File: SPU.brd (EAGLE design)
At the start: 160 x 130 mm, 421 parts, among them Q1 BSS123, Q2 12MHz, Q3 BSS123, Q4 BSS123, Q5 BSS123, Q6 BSS123, Y1 32.768kHz

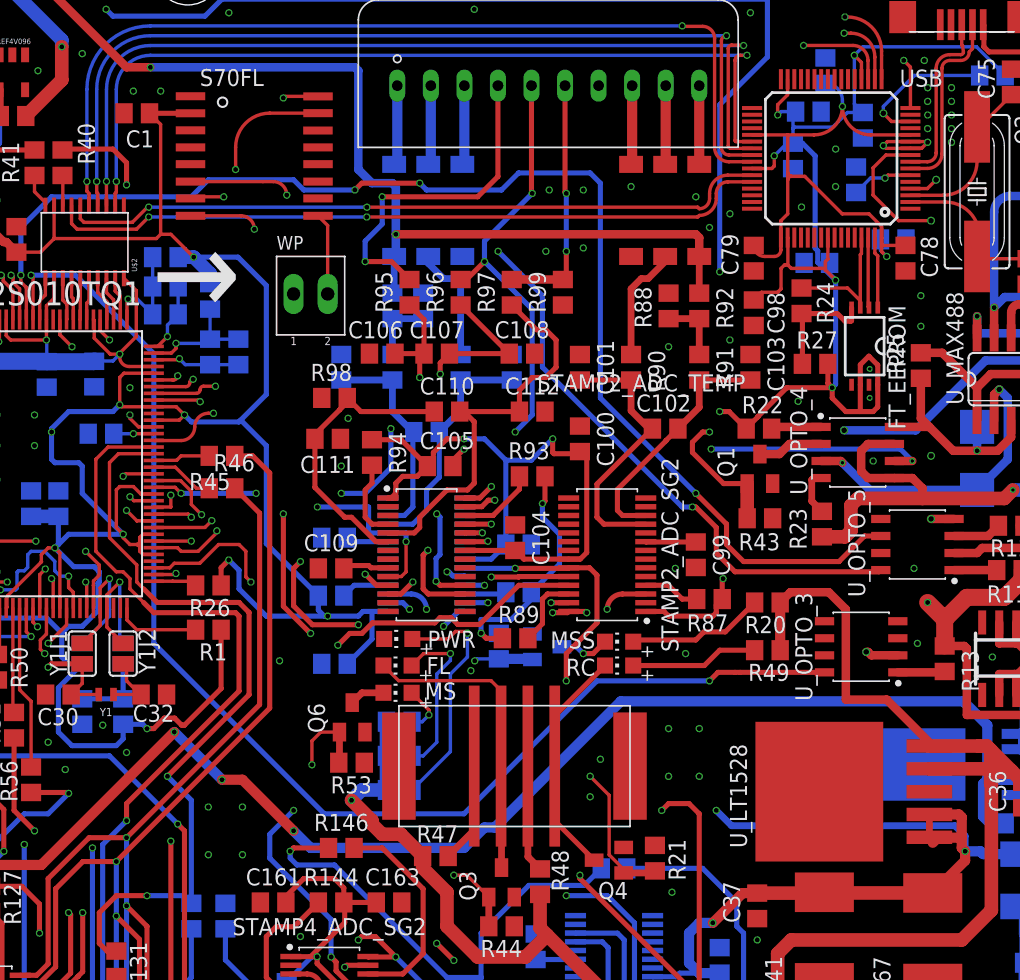
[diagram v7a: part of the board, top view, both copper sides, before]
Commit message: Minor changes
- XTAL from AUX to MAIN
- Removes authors
- Adds interface measurements
- Fixes Airwire / Wirestub
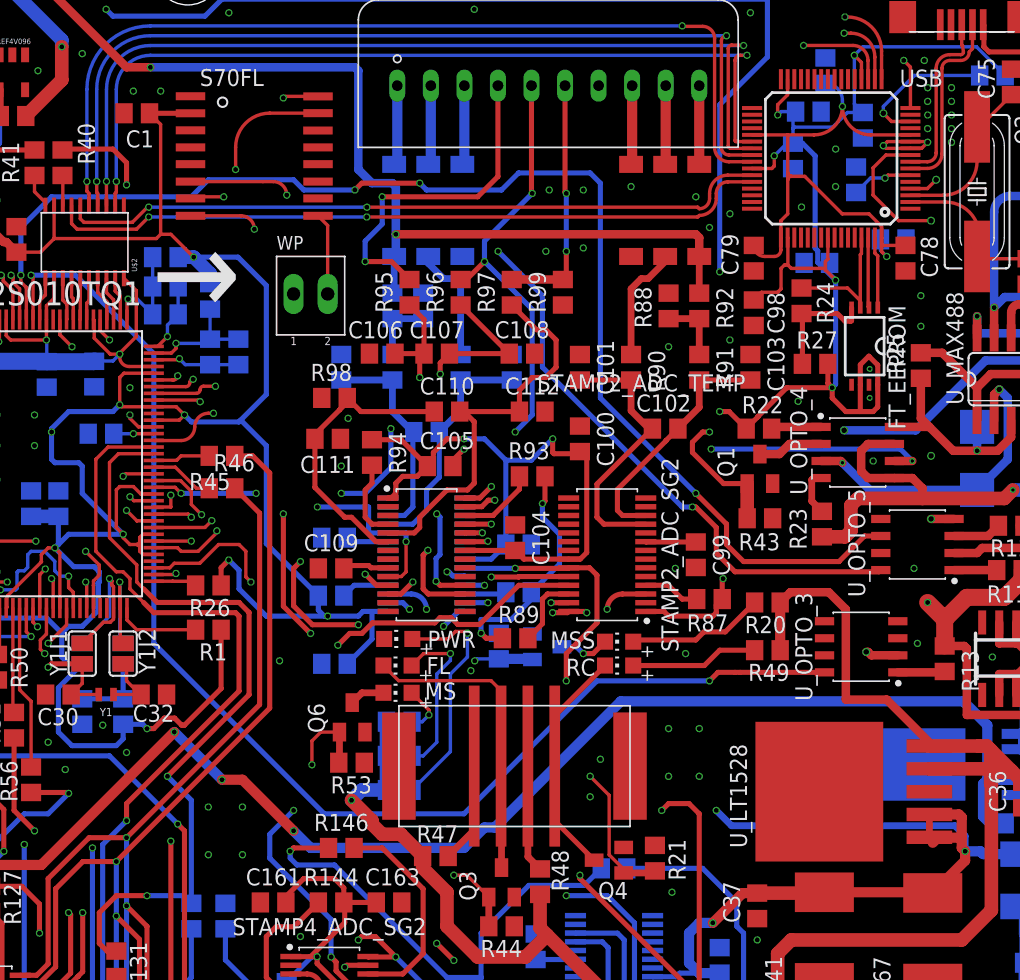
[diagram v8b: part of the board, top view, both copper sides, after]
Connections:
- removed net AUX_EXTAL: RCJ1.1, SF2_M2S010TQ1.69, Y1J2.2
- removed net AUX_XTAL: RCJ2.1, SF2_M2S010TQ1.68, Y1J1.1
- new net MAIN_EXTAL: RCJ1.1, SF2_M2S010TQ1.71, Y1J2.2
- new net MAIN_XTAL: RCJ2.1, SF2_M2S010TQ1.70, Y1J1.1
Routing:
- net MAIN_XTAL: track 0.00 -> 11.9 mm, vias 0 -> 1
- net AUX_XTAL: track 11.3 -> 0.00 mm, vias 1 -> 0
- net AUX_EXTAL: track 10.1 -> 0.00 mm, vias 1 -> 0
- net MAIN_EXTAL: track 0.00 -> 9.35 mm, vias 0 -> 1
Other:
- board text removed: "J. Lusky, R. Grimsmann"
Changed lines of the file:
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@@
 <setting verticaltext="up"/>
 </settings>
-<grid distance="10" unitdist="mil" unit="mil" style="lines" multiple="1" display="yes" altdistance="1" altunitdist="mil" altunit="mil"/>
+<grid distance="0.1" unitdist="mm" unit="mm" style="lines" multiple="1" display="yes" altdistance="1" altunitdist="mil" altunit="mil"/>
 <layers>
 <layer number="1" name="Top" color="4" fill="1" visible="yes" active="yes"/>
@@
 <dimension x1="160" y1="130" x2="160.02" y2="0" x3="182.870196875" y3="65.003515625" textsize="1.778" layer="47"/>
 <dimension x1="0" y1="0" x2="160" y2="0" x3="80" y3="-17.78" textsize="1.778" layer="47"/>
-<dimension x1="88.9" y1="1.27" x2="99.695" y2="1.27" x3="94.2975" y3="-5.08" textsize="1.778" layer="47"/>
 <dimension x1="156.21" y1="75.692" x2="156.21" y2="114.935" x3="175.26" y3="95.3135" textsize="1.778" layer="47"/>
 <dimension x1="0" y1="0" x2="5" y2="5" x3="-3.81" y3="2.5" textsize="1.778" layer="47" dtype="vertical"/>
@@
 <wire x1="160.02" y1="129.54" x2="160.02" y2="123.19" width="0.1524" layer="21"/>
 <wire x1="160.02" y1="123.19" x2="0" y2="123.19" width="0.1524" layer="21"/>
-<dimension x1="143.002" y1="127.762" x2="132.207" y2="127.7366" x3="137.58531875" y3="135.899965625" textsize="1.778" layer="47"/>
-<text x="150.622" y="3.302" size="1.778" layer="22" rot="MR0">J. Lusky, R. Grimsmann</text>
+<dimension x1="143.002" y1="127.762" x2="132.207" y2="127.762" x3="137.6045" y3="135.382046875" textsize="1.778" layer="47"/>
 <text x="21.59" y="3.302" size="1.778" layer="22" rot="MR0">Nov. 2021</text>
 <text x="6.858" y="119.126" size="1.778" layer="22" rot="MR270">Short 5V - GND to activate FLOMESS MODE</text>
+<dimension x1="160" y1="127.762" x2="143" y2="127.762" x3="151.5" y3="135.382046875" textsize="1.778" layer="47"/>
+<dimension x1="159" y1="115" x2="159" y2="130" x3="175.2854" y3="122.5" textsize="1.778" layer="47"/>
 </plain>
 <attributes>
@@
 <wire x1="45.532" y1="65.024" x2="44.323" y2="66.233" width="0.381" layer="1"/>
 <wire x1="44.323" y1="66.233" x2="44.323" y2="70.485" width="0.381" layer="1"/>
-<wire x1="134.1628" y1="56.334" x2="134.112" y2="56.3848" width="0.381" layer="1"/>
 <wire x1="51.67544375" y1="84.7677" x2="51.4597" y2="84.98344375" width="0.381" layer="1"/>
 <wire x1="51.4597" y1="84.98344375" x2="51.4597" y2="86.58855625" width="0.381" layer="1"/>
@@
 <wire x1="99.314" y1="90.17" x2="100.584" y2="90.17" width="0.381" layer="1"/>
 <wire x1="137.922" y1="59.436" x2="137.922" y2="58.747" width="0.762" layer="1"/>
-<wire x1="137.922" y1="58.747" x2="135.509" y2="56.334" width="0.762" layer="1"/>
 <wire x1="128.778" y1="56.3848" x2="127.4318" y2="56.3848" width="1.016" layer="1"/>
 <wire x1="43.434" y1="99.23714375" x2="43.434" y2="101.798" width="0.381" layer="1"/>
@@
 <wire x1="128.8288" y1="56.334" x2="128.778" y2="56.3848" width="1.016" layer="1"/>
 <wire x1="127.4826" y1="56.334" x2="127.4318" y2="56.3848" width="1.016" layer="1"/>
-<wire x1="135.509" y1="56.334" x2="127.4826" y2="56.334" width="1.016" layer="1"/>
-<wire x1="135.509" y1="56.334" x2="134.1628" y2="56.334" width="0" layer="19" extent="1-1"/>
+<wire x1="137.922" y1="58.747" x2="135.509" y2="56.334" width="0.762" layer="1"/>
+<wire x1="127.4318" y1="56.3848" x2="135.4582" y2="56.3848" width="0.762" layer="1"/>
+<wire x1="135.4582" y1="56.3848" x2="135.509" y2="56.334" width="0.762" layer="1"/>
 </signal>
 <signal name="1V2">
@@
 <contactref element="U$9" pad="P$2"/>
 <contactref element="CON_STAMP2" pad="P$3"/>
-<wire x1="100.61" y1="110.772" x2="100.61" y2="110.77" width="0.762" layer="16"/>
-<wire x1="100.61" y1="110.77" x2="100.5205" y2="110.6805" width="0.762" layer="16"/>
-<wire x1="100.61" y1="110.772" x2="100.457" y2="110.619" width="0.762" layer="16"/>
-<wire x1="100.61" y1="116.487" x2="100.61" y2="110.772" width="0.762" layer="16"/>
+<wire x1="100.61" y1="116.487" x2="100.61" y2="110.77" width="0.762" layer="16"/>
+<wire x1="100.61" y1="110.77" x2="100.459" y2="110.619" width="0.254" layer="16"/>
+<wire x1="100.459" y1="110.619" x2="100.457" y2="110.619" width="0.254" layer="16"/>
 </signal>
 <signal name="STAMP2_SG1_AIN2">
@@
 <wire x1="76.52" y1="71.12" x2="74.464" y2="71.12" width="0.254" layer="1"/>
 </signal>
-<signal name="AUX_EXTAL">
-<contactref element="SF2_M2S010TQ1" pad="69"/>
+<signal name="MAIN_EXTAL">
 <contactref element="Y1J2" pad="2"/>
 <contactref element="RCJ1" pad="1"/>
-<wire x1="73.97" y1="77.56" x2="73.97" y2="76.144" width="0.254" layer="1"/>
-<wire x1="73.97" y1="76.144" x2="75.184" y2="74.93" width="0.254" layer="1"/>
-<wire x1="73.97" y1="77.56" x2="73.97" y2="78.542" width="0.254" layer="1"/>
-<wire x1="73.97" y1="78.542" x2="74.93" y2="79.502" width="0.254" layer="1"/>
 <via x="74.93" y="79.502" extent="1-16" drill="0.35"/>
 <wire x1="74.93" y1="79.502" x2="74.93" y2="75.184" width="0.254" layer="16"/>
 <wire x1="74.93" y1="75.184" x2="75.184" y2="74.93" width="0.254" layer="16"/>
+<contactref element="SF2_M2S010TQ1" pad="71"/>
+<wire x1="75.184" y1="74.93" x2="74.97" y2="75.144" width="0.254" layer="1"/>
+<wire x1="74.97" y1="75.144" x2="74.97" y2="77.56" width="0.254" layer="1"/>
+<wire x1="74.97" y1="77.56" x2="74.93" y2="77.6" width="0.254" layer="1"/>
+<wire x1="74.93" y1="77.6" x2="74.93" y2="79.502" width="0.254" layer="1"/>
 </signal>
-<signal name="AUX_XTAL">
-<contactref element="SF2_M2S010TQ1" pad="68"/>
+<signal name="MAIN_XTAL">
 <contactref element="Y1J1" pad="1"/>
 <contactref element="RCJ2" pad="1"/>
-<wire x1="73.47" y1="77.56" x2="73.47" y2="76.264" width="0.254" layer="1"/>
-<wire x1="73.47" y1="76.264" x2="72.136" y2="74.93" width="0.254" layer="1"/>
-<wire x1="73.47" y1="77.56" x2="73.47" y2="79.058" width="0.254" layer="1"/>
-<wire x1="73.47" y1="79.058" x2="74.168" y2="79.756" width="0.254" layer="1"/>
 <via x="74.168" y="79.756" extent="1-16" drill="0.35"/>
-<wire x1="74.168" y1="79.756" x2="74.168" y2="77.47" width="0.254" layer="16"/>
-<wire x1="74.168" y1="77.47" x2="74.168" y2="76.962" width="0.254" layer="16"/>
+<wire x1="74.168" y1="79.756" x2="74.168" y2="76.962" width="0.254" layer="16"/>
 <wire x1="74.168" y1="76.962" x2="72.136" y2="74.93" width="0.254" layer="16"/>
+<contactref element="SF2_M2S010TQ1" pad="70"/>
+<wire x1="73.7112" y1="76.5052" x2="74.23125" y2="76.5052" width="0.254" layer="1"/>
+<wire x1="74.23125" y1="76.5052" x2="74.47" y2="76.74395" width="0.254" layer="1"/>
+<wire x1="74.47" y1="76.74395" x2="74.47" y2="77.56" width="0.254" layer="1"/>
+<wire x1="72.136" y1="74.93" x2="73.7112" y2="76.5052" width="0.254" layer="1"/>
+<wire x1="74.168" y1="79.756" x2="74.3486" y2="79.5754" width="0.254" layer="1"/>
+<wire x1="74.3486" y1="79.5754" x2="74.3486" y2="79.261175" width="0.254" layer="1"/>
+<wire x1="74.3486" y1="79.261175" x2="74.47" y2="79.139775" width="0.254" layer="1"/>
+<wire x1="74.47" y1="79.139775" x2="74.47" y2="77.56" width="0.254" layer="1"/>
 </signal>
 <signal name="NET_U">
